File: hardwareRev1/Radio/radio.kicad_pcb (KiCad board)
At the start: 2 copper layers, 57 parts, among them U1 AX503, U2 PE42424, U3 RF5110G, X1 TCXO

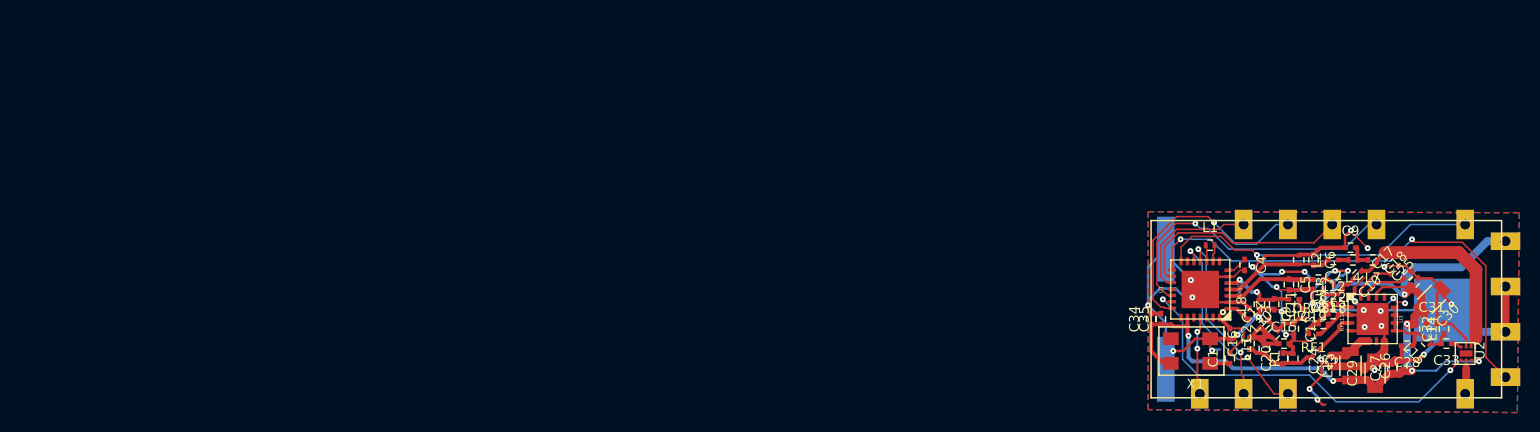
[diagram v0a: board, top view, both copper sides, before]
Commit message: Finished the PCB for the new radio module.
Still needs to be checked.
Added the datasheet for the amp and switch
Added the footprint for a 1.27mm pitch 2X8 connector
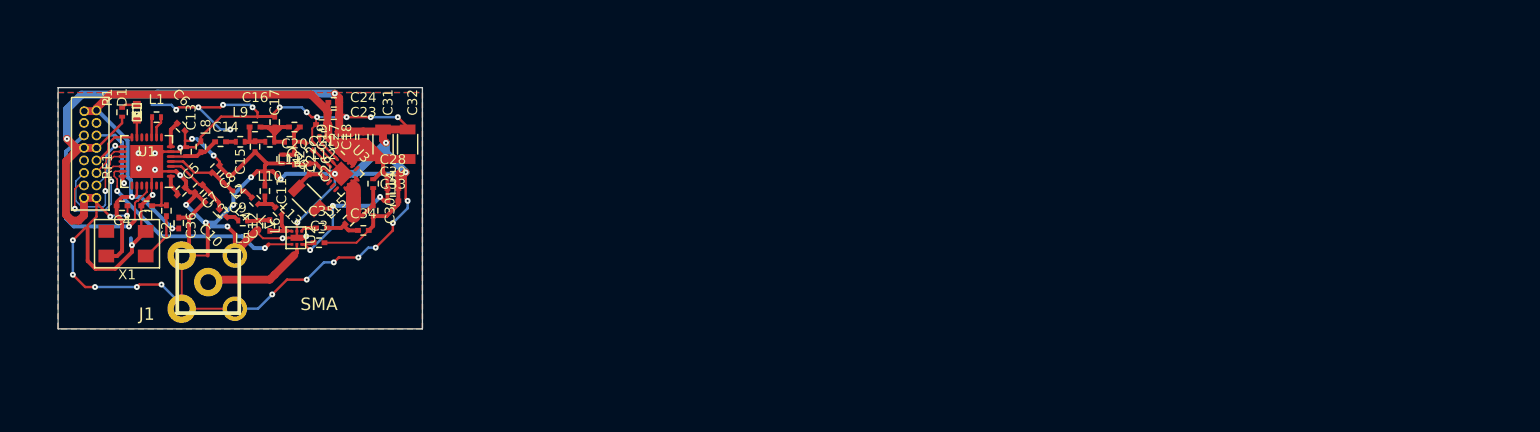
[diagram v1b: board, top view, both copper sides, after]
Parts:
- removed G***: LOGO, hardwareRev1:TREX
- added C36: 100pf, Capacitors_SMD:C_0402, F.Cu at (79.2, 66.2)
- added D1: LED, LEDs:LED-0603, F.Cu at (75.0, 55.0)
- added J1: SMA, hardwareRev1:SMA, F.Cu at (82.2, 72.2)
- added R2: 180, Resistors_SMD:R_0402, F.Cu at (89.8, 59.8)
- C10, C9: value 12pf -> 10pf
- C11: value 2.2pf -> 12pf
- C12: value 22pf -> 12pf
- C13: value 33pf -> 2.2pf
- C14: value 4.7pf -> 22pf
- C15: value 47pf -> 33pf
- C16: value 1.8pf -> 4.7pf
- C17, C27: value 10nf -> 47pf
- C18, C21: value 1nf -> 10nf
- C19: value 10nf -> 1nf
- C20: value 15pf -> 1.8pf
- C22: value 27pf -> 15pf
- C23, C28: value C -> 1nf
- C25: value 47pf -> 100pf
- C26: value 1nf -> 27pf
- C29: value 3.3uf -> 10nf; footprint Capacitors_SMD:C_1206 -> Capacitors_SMD:C_0402
- C3: value C -> 1uf
- C30: value 3.3uf -> 33pf; footprint Capacitors_SMD:C_1206 -> Capacitors_SMD:C_0402
- C31: value 1nf -> 3.3uf; footprint Capacitors_SMD:C_0402 -> Capacitors_SMD:C_1206
- C32: value 56pf -> 3.3uf; footprint Capacitors_SMD:C_0402 -> Capacitors_SMD:C_1206
- C33: value 100pf -> 1nf
- C34: value 1uf -> 56pf
- C4: value C -> 100pf
- C5, C6: value 10pf -> C
- L1: value INDUCTOR -> 60nh
- RF1: value DRA818 -> RFConn; footprint hardwareRev1:RFModuleOutline -> hardwareRev1:1.27mm2X8; moved to F.Cu
- U1: footprint w_smd_qfn:qfn-28 -> Housings_DFN_QFN:QFN-28-1EP_5x5mm_Pitch0.5mm
- U2: footprint hardwareRev1:PE4242 -> PE4242
- U3: footprint w_smd_qfn:qfn-16 -> Housings_DFN_QFN:QFN-16-1EP_3x3mm_Pitch0.5mm
- X1: footprint hardwareRev1:FOX924B -> FOX924B
- moved R1 121.5 mm to (73.5, 55.0)
- moved U2 119.3 mm to (91.2, 67.8)
- moved C6 115.8 mm to (79.5, 56.5), turned to 315 degrees
- moved C7 115.5 mm to (81.2, 62.8), turned to 225 degrees
- moved C10 115.4 mm to (83.8, 65.2), turned to 135 degrees
- moved C17 114.7 mm to (89.0, 56.0), turned to 90 degrees
- moved C4 114.2 mm to (73.5, 64.5), turned to 0 degrees
- moved C9 113.1 mm to (85.2, 63.0), turned to 180 degrees
- moved C25 113.1 mm to (92.5, 58.5), turned to 135 degrees
- moved C5 112.9 mm to (79.5, 63.0), turned to 225 degrees
- moved C26 112.8 mm to (92.5, 60.8), turned to 270 degrees
- moved C8 112.6 mm to (83.0, 60.8), turned to 225 degrees
- moved C13 112.5 mm to (81.5, 58.5), turned to 90 degrees
- moved L4 111.7 mm to (87.0, 64.0), turned to 135 degrees
- moved L3 111.6 mm to (82.2, 63.8), turned to 225 degrees
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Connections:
- C1 pad 2: Net-(C1-Pad2) -> GND
- C11 pad 1: /PA/PAInput -> GND
- C11 pad 2: GND -> Net-(C11-Pad2)
- C12 pad 2: /PA/PAInput -> Net-(C12-Pad2)
- C13 pad 1: Net-(C13-Pad1) -> /PA/PAInput
- C14 pad 2: Net-(C13-Pad1) -> /PA/PAInput
- C15 pad 1: Net-(C14-Pad1) -> Net-(C15-Pad1)
- C16 pad 2: Net-(C14-Pad1) -> Net-(C15-Pad1)
- C17 pad 1: Net-(C17-Pad1) -> Net-(C16-Pad1)
- C18 pad 1: Net-(C18-Pad1) -> +3.3V
- C2 pad 1: Net-(C1-Pad2) -> Net-(C2-Pad1)
- C2 pad 2: GND -> Net-(C1-Pad1)
- C20 pad 1: Net-(C16-Pad1) -> Net-(C20-Pad1)
- C20 pad 2: GND -> Net-(C16-Pad1)
- C22 pad 1: +3.3V -> Net-(C20-Pad1)
- C23 pad 1: Net-(C23-Pad1) -> +3.3V
- C23 pad 2: Net-(C16-Pad1) -> GND
- C24 pad 1: GND -> +3.3V
- C24 pad 2: Net-(C24-Pad2) -> GND
- C25 pad 1: +3.3V -> Net-(C25-Pad1)
- C25 pad 2: GND -> Net-(C20-Pad1)
- C26 pad 1: +3.3V -> GND
- C26 pad 2: GND -> Net-(C26-Pad2)
- C28 pad 1: Net-(C28-Pad1) -> +3.3V
- C3 pad 1: GND -> +3.3V
- C3 pad 2: Net-(C3-Pad2) -> GND
- C30 pad 1: GND -> Net-(C30-Pad1)
- C30 pad 2: +3.3V -> GND
- C32 pad 1: Net-(C32-Pad1) -> GND
- C32 pad 2: GND -> +3.3V
- C33 pad 1: /PA/PAOutput -> +3.3V
- C33 pad 2: Net-(C32-Pad1) -> GND
- C34 pad 1: +3.3V -> Net-(C34-Pad1)
- C35 pad 1: +3.3V -> /PA/PAOutput
- C35 pad 2: GND -> Net-(C34-Pad1)
- C4 pad 1: Net-(C4-Pad1) -> +3.3V
- C5 pad 1: Net-(C5-Pad1) -> GND
- C5 pad 2: GND -> Net-(C5-Pad2)
- C6 pad 1: GND -> Net-(C6-Pad1)
- C6 pad 2: Net-(C6-Pad2) -> GND
- C7 pad 1: Net-(C7-Pad1) -> Net-(C10-Pad2)
- C7 pad 2: Net-(C6-Pad2) -> GND
- C8 pad 1: Net-(C8-Pad1) -> GND
- C8 pad 2: Net-(C5-Pad1) -> Net-(C8-Pad2)
- C9 pad 1: GND -> Net-(C9-Pad1)
- C9 pad 2: Net-(C9-Pad2) -> Net-(C8-Pad2)
- L10 pad 1: Net-(C14-Pad1) -> Net-(C16-Pad1)
- L10 pad 2: Net-(C13-Pad1) -> Net-(C15-Pad1)
- L11 pad 1: Net-(C16-Pad1) -> Net-(C20-Pad1)
- L11 pad 2: Net-(C14-Pad1) -> Net-(C16-Pad1)
- L13 pad 2: Net-(C24-Pad2) -> Net-(C26-Pad2)
- L14 pad 2: Net-(C28-Pad1) -> Net-(C30-Pad1)
- L15 pad 1: Net-(C32-Pad1) -> Net-(C34-Pad1)
- L15 pad 2: Net-(C28-Pad1) -> Net-(C30-Pad1)
- L2 pad 2: Net-(C6-Pad2) -> Net-(C8-Pad2)
- L3 pad 1: Net-(C5-Pad1) -> Net-(C10-Pad2)
- L4 pad 1: Net-(C9-Pad2) -> Net-(C11-Pad2)
- L4 pad 2: Net-(C7-Pad1) -> Net-(C9-Pad1)
- L5 pad 1: Net-(C10-Pad2) -> Net-(C12-Pad2)
- L5 pad 2: Net-(C8-Pad1) -> Net-(C10-Pad1)
- L6 pad 1: Net-(C10-Pad2) -> Net-(C12-Pad2)
- L7 pad 1: Net-(C10-Pad1) -> Net-(C12-Pad1)
- L7 pad 2: Net-(C9-Pad2) -> Net-(C11-Pad2)
- L9 pad 1: Net-(C13-Pad1) -> Net-(C15-Pad1)
- L9 pad 2: Net-(C12-Pad1) -> Net-(C14-Pad1)
- R1 pad 1: Net-(C16-Pad1) -> GND
- R1 pad 2: GND -> Net-(D1-Pad2)
- RF1 pad 10: GND -> /CLK
- RF1 pad 11: /CLK -> /MISO
- RF1 pad 12: Net-(RF1-Pad12) -> /SEL
- RF1 pad 16: /UART_RX -> +3.3V
- RF1 pad 2: /MOSI -> (no net)
- RF1 pad 3: /AF_OUT -> /AF_IN
- RF1 pad 4: /MISO -> GND
- RF1 pad 5: /IRQOUT -> (no net)
- RF1 pad 7: /SEL -> /IRQOUT
- RF1 pad 8: +3.3V -> GND
- U1 pad 1: Net-(C3-Pad2) -> Net-(C5-Pad2)
- U1 pad 11: /UART_TX -> (no net)
- U1 pad 12: /UART_RX -> (no net)
- U1 pad 13: (no net) -> Net-(D1-Pad1)
- U1 pad 26: (no net) -> GND
- U1 pad 28: Net-(C1-Pad2) -> Net-(C1-Pad1)
- U1 pad 3: Net-(C5-Pad1) -> Net-(C10-Pad2)
- U1 pad 4: Net-(C6-Pad2) -> Net-(C8-Pad2)
- U1 pad 7: Net-(C4-Pad1) -> Net-(C6-Pad1)
- U2 pad 2: Net-(RF1-Pad12) -> Net-(J1-Pad1)
- U2 pad 4: Net-(C10-Pad1) -> /PA/PAOutput
- U2 pad 6: /PA/PAOutput -> Net-(C12-Pad1)
- U3 pad 10: Net-(C28-Pad1) -> Net-(C30-Pad1)
- U3 pad 11: Net-(C28-Pad1) -> Net-(C30-Pad1)
- U3 pad 12: Net-(C28-Pad1) -> Net-(C30-Pad1)
- U3 pad 15: Net-(C18-Pad1) -> +3.3V
- U3 pad 16: Net-(C17-Pad1) -> +3.3V
- U3 pad 3: Net-(C23-Pad1) -> Net-(C25-Pad1)
- U3 pad 5: Net-(C24-Pad2) -> Net-(C26-Pad2)
- U3 pad 6: Net-(C24-Pad2) -> Net-(C26-Pad2)
- U3 pad 8: GND -> (no net)
- U3 pad 9: Net-(C28-Pad1) -> Net-(C30-Pad1)
- X1 pad 3: Net-(C1-Pad1) -> Net-(C2-Pad1)
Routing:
- net GND: track 212.8 -> 331.1 mm, vias 32 -> 49
- net /CLK: track 49.5 -> 5.61 mm, vias 2 -> 1
- net /SEL: track 33.4 -> 4.98 mm, vias 1 -> 0
- net /UART_RX: track 21.2 -> 0.00 mm, vias 2 -> 0
- net +3.3V: track 94.1 -> 113.7 mm, vias 7 -> 5
- net Net-(C10-Pad1): track 21.3 -> 2.11 mm
- net /UART_TX: track 19.1 -> 0.00 mm, vias 2 -> 0
- net /IRQOUT: track 31.5 -> 12.6 mm, vias 1 -> 2
- net /MISO: track 22.4 -> 3.80 mm
- net /AF_OUT: track 25.8 -> 7.86 mm
- net /TXRX: track 40.0 -> 23.3 mm
- net /AF_IN: track 9.38 -> 21.4 mm, vias 2 -> 1
- net Net-(C6-Pad2): track 11.6 -> 0.00 mm
- net Net-(J1-Pad1): track 0.00 -> 11.1 mm
- net Net-(C5-Pad1): track 10.9 -> 0.00 mm
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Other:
- board outline added: 37 x 24.5 mm
- net class Default: clearance 0.2 -> 0.1524; trace_width 0.25 -> 0.1524
- rule trace_clearance: 0.2 -> 0.1524
- rule trace_min: 0.153 -> 0.1524
- board text removed: "AB1TJ RF MODULE REV0.TREX"

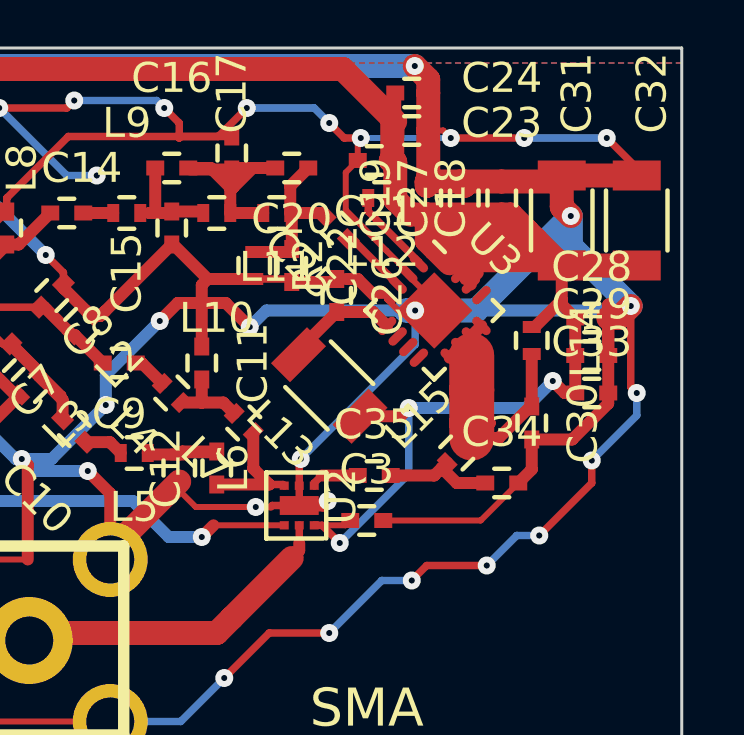
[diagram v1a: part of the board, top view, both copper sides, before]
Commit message: Added a capacitor to the power amp sheet in order to facilitate 440.
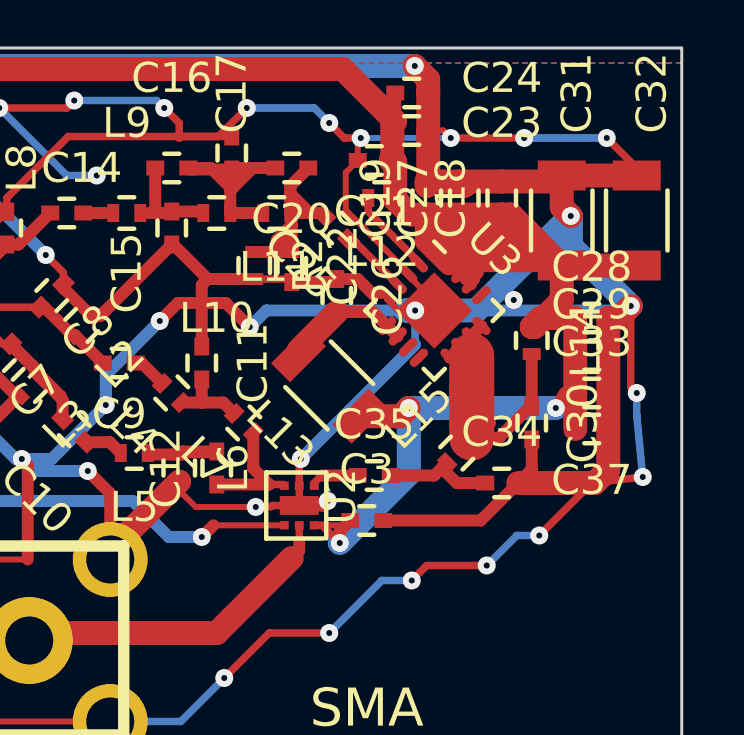
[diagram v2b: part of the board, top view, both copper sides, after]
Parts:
- added C37: C, Capacitors_SMD:C_0402, F.Cu at (101.0, 65.2)
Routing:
- net +3.3V: track 113.7 -> 120.8 mm
- net GND: track 331.1 -> 335.4 mm, vias 49 -> 50
- net Net-(C20-Pad1): track 5.47 -> 8.33 mm
- net Net-(C26-Pad2): track 3.82 -> 4.32 mm

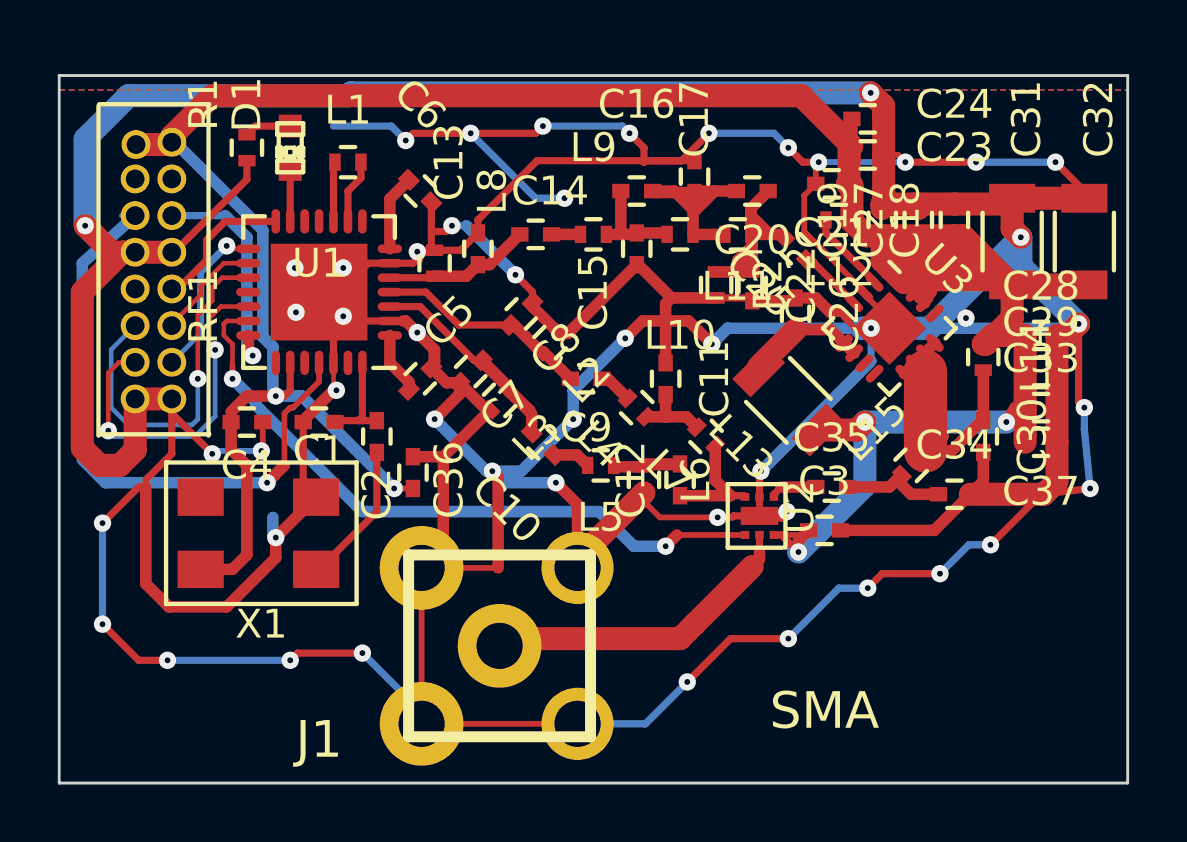
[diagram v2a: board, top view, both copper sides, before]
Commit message: Rerouted some power traces. Need to rerout it again.
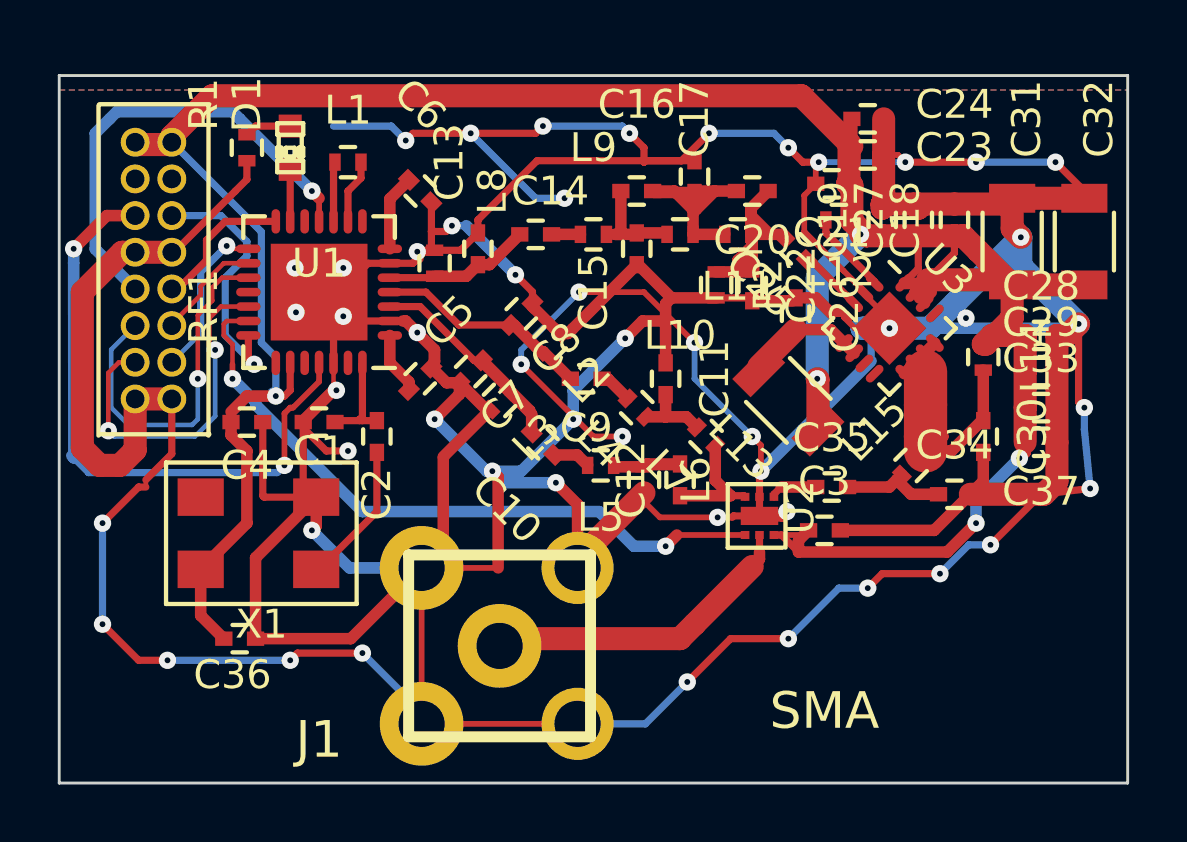
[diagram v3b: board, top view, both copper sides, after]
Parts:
- RF1: footprint hardwareRev1:1.27mm2X8 -> 1.27mm2X8
- moved C36 8.31 mm to (73.2, 72.0), turned to 180 degrees
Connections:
- RF1 pad 5: (no net) -> /DATA
- U1 pad 11: (no net) -> /DATA
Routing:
- net GND: track 335.4 -> 318.7 mm, vias 50 -> 51
- net /DATA: track 0.00 -> 16.1 mm, vias 0 -> 1
- net +3.3V: track 120.8 -> 111.0 mm
- net /AF_OUT: track 7.86 -> 9.03 mm
- net /AF_IN: track 21.4 -> 22.1 mm, vias 1 -> 2

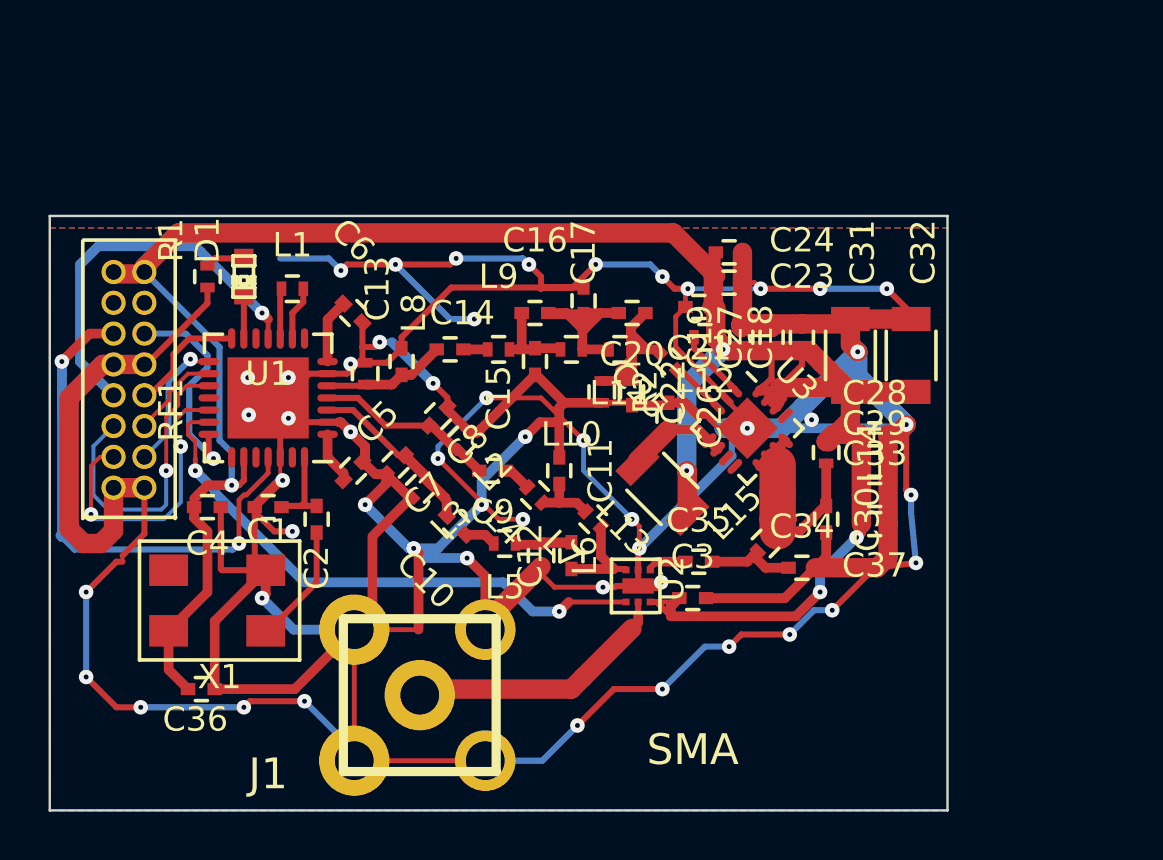
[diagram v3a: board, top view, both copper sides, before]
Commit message: Finished the new radio module schematic.
Added a MCU beacause having 4 layers is an auful waste of space.
Added a GPS
Added an edge mount SMA component.
Added the NEO-7 hardware integration manual.
Need to finish the schematic.
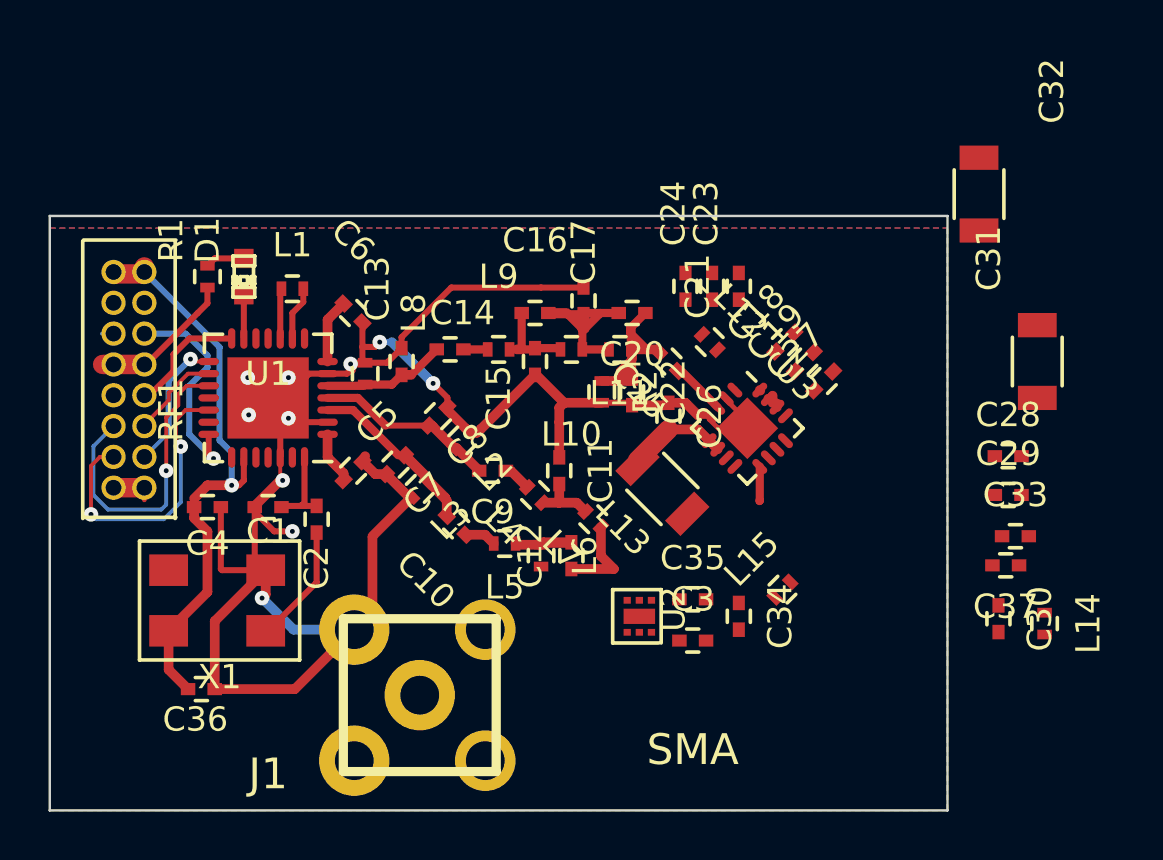
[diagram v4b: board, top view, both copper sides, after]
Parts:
- moved L14 11.4 mm to (108.0, 69.3)
- moved C32 8.50 mm to (105.3, 51.6)
- moved C30 8.20 mm to (106.1, 69.1)
- moved C33 6.04 mm to (106.8, 65.7)
- moved C37 5.66 mm to (106.4, 66.9)
- moved C29 5.64 mm to (106.5, 64.0)
- moved C28 5.57 mm to (106.5, 62.4)
- moved C31 5.21 mm to (107.7, 58.5)
- moved C34 3.28 mm to (95.4, 69.0), turned to 270 degrees
- moved C27 2.80 mm to (98.9, 59.3), turned to 45 degrees
- moved C19 2.79 mm to (98.1, 58.5), turned to 45 degrees
- moved C24 2.28 mm to (93.2, 55.4), turned to 90 degrees
- moved L15 2.02 mm to (97.2, 67.9)
- moved C21 1.86 mm to (95.4, 55.4), turned to 90 degrees
- moved C3 1.75 mm to (93.5, 70.0)
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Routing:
- net GND: track 318.7 -> 94.6 mm, vias 51 -> 10
- net +3.3V: track 111.0 -> 25.4 mm, vias 5 -> 1
- net /TXRX: track 23.3 -> 0.00 mm, vias 2 -> 0
- net /AF_IN: track 22.1 -> 0.48 mm, vias 2 -> 0
- net /DATA: track 16.1 -> 0.00 mm, vias 1 -> 0
- net Net-(J1-Pad1): track 11.1 -> 0.35 mm
- net Net-(C30-Pad1): track 11.1 -> 1.43 mm
- net Net-(C34-Pad1): track 3.72 -> 0.00 mm
- net Net-(L12-Pad2): track 2.88 -> 0.04 mm
- net /PA/PAOutput: track 1.64 -> 0.00 mm
- net Net-(C12-Pad1): track 4.22 -> 3.70 mm
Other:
- copper layers 2 -> 4
